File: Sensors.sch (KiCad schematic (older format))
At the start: 11 parts, among them Q20 2N7002K, Q21 2N7002K, U12 SHTC3

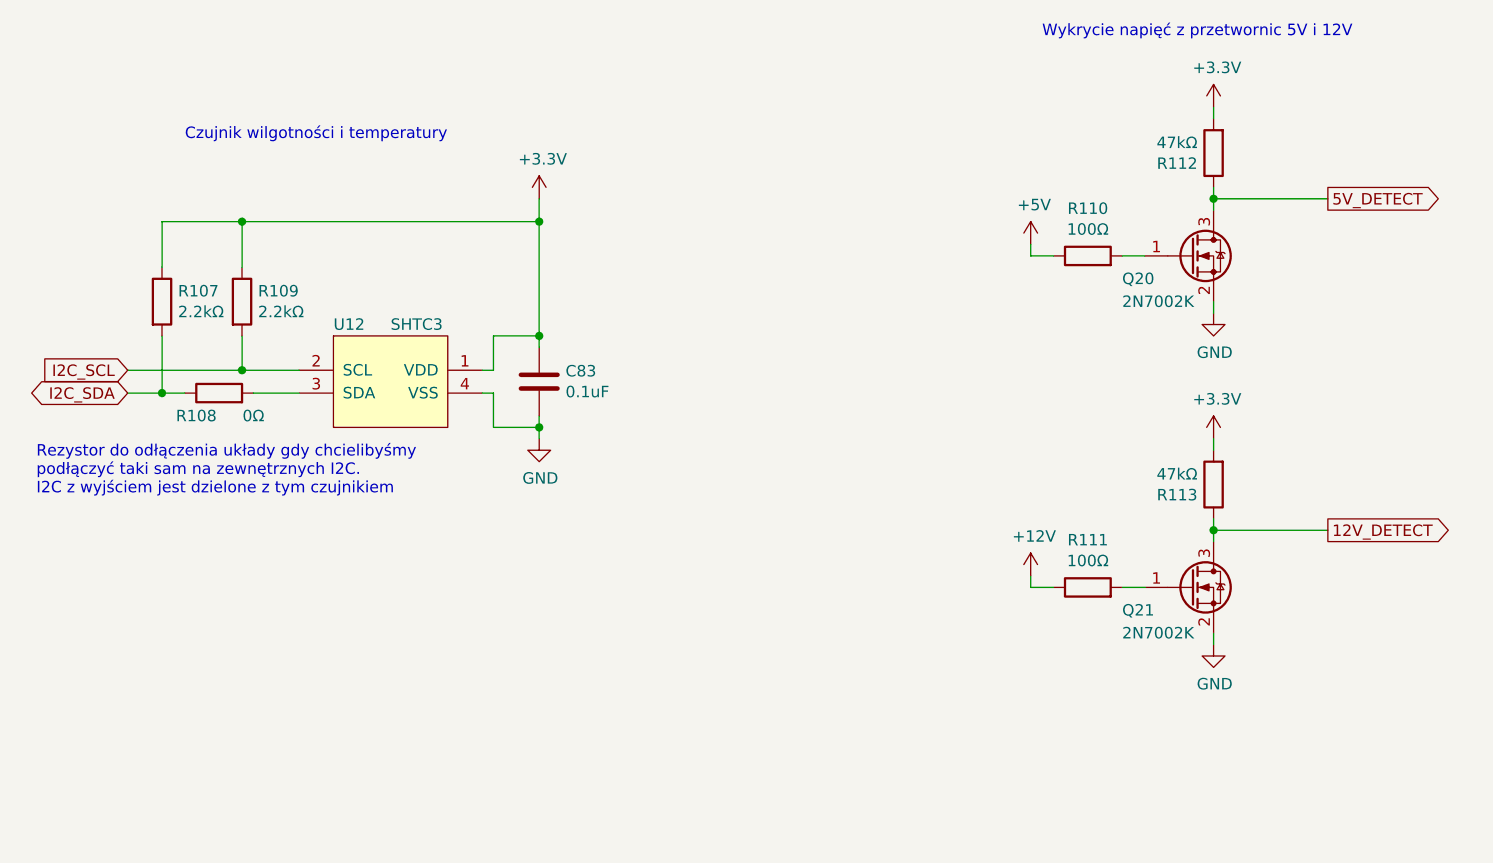
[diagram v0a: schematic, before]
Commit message: Improve ESD Protection for TMC2209, Fuses. Schematic ready v1
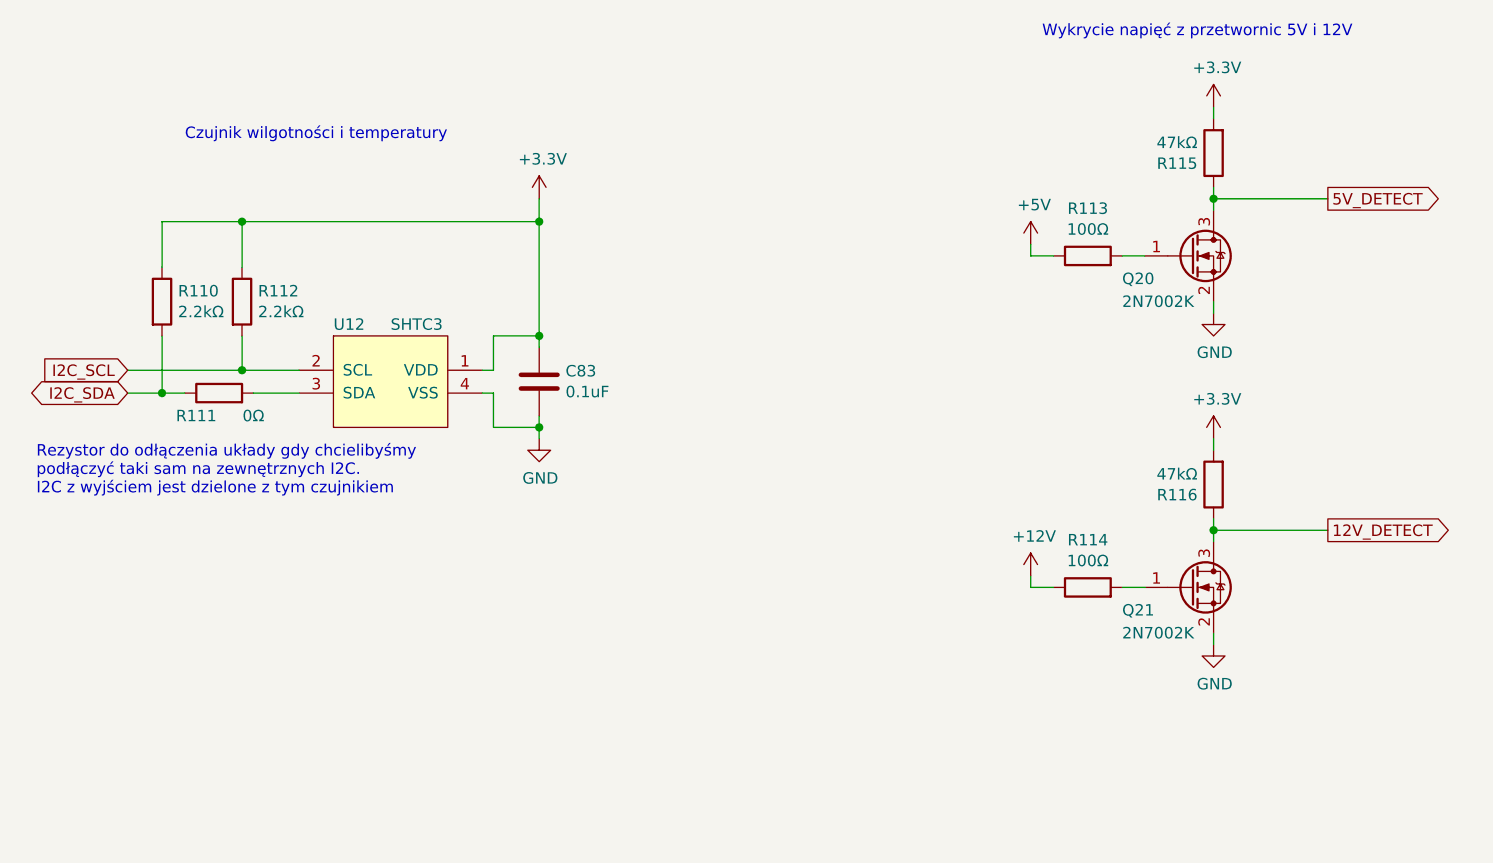
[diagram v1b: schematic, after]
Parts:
- renumbered R107 to R110, R108 to R111, R109 to R112, R110 to R113, R111 to R114, R112 to R115, R113 to R116
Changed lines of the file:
@@
 $EndComp
 $Comp
-L power:GND #PWR0217
+L power:GND #PWR0208
 U 1 1 5E15EB06
 P 3900 2700
-F 0 "#PWR0217" H 3900 2450 50  0001 C CNN
+F 0 "#PWR0208" H 3900 2450 50  0001 C CNN
 F 1 "GND" H 3905 2527 50  0000 C CNN
 F 2 "" H 3900 2700 50  0001 C CNN
@@
 $EndComp
 $Comp
-L power:+3.3V #PWR0216
+L power:+3.3V #PWR0207
 U 1 1 5E15FDB5
 P 3900 1650
-F 0 "#PWR0216" H 3900 1500 50  0001 C CNN
+F 0 "#PWR0207" H 3900 1500 50  0001 C CNN
 F 1 "+3.3V" H 3915 1823 50  0000 C CNN
 F 2 "" H 3900 1650 50  0001 C CNN
@@
 AR Path="/5E91D7CC/5E1C6F9E" Ref="R?"  Part="1"
 AR Path="/5E91D96F/5E1C6F9E" Ref="R?"  Part="1"
-AR Path="/5E1B3A8F/5E1C6F9E" Ref="R109"  Part="1"
-F 0 "R109" H 2670 2146 50  0000 L CNN
+AR Path="/5E1B3A8F/5E1C6F9E" Ref="R112"  Part="1"
+F 0 "R112" H 2670 2146 50  0000 L CNN
 F 1 "2.2kΩ" H 2670 2055 50  0000 L CNN
 F 2 "Resistor_SMD:R_0603_1608Metric" V 2530 2100 50  0001 C CNN
@@
 AR Path="/5E91D7CC/5E1C6FA4" Ref="R?"  Part="1"
 AR Path="/5E91D96F/5E1C6FA4" Ref="R?"  Part="1"
-AR Path="/5E1B3A8F/5E1C6FA4" Ref="R107"  Part="1"
-F 0 "R107" H 2320 2146 50  0000 L CNN
+AR Path="/5E1B3A8F/5E1C6FA4" Ref="R110"  Part="1"
+F 0 "R110" H 2320 2146 50  0000 L CNN
 F 1 "2.2kΩ" H 2320 2055 50  0000 L CNN
 F 2 "Resistor_SMD:R_0603_1608Metric" V 2180 2100 50  0001 C CNN
@@
 P 6850 1250
 AR Path="/5DFB2EC0/5E1CAE31" Ref="#PWR?"  Part="1"
-AR Path="/5E1B3A8F/5E1CAE31" Ref="#PWR0220"  Part="1"
-F 0 "#PWR0220" H 6850 1100 50  0001 C CNN
+AR Path="/5E1B3A8F/5E1CAE31" Ref="#PWR0211"  Part="1"
+F 0 "#PWR0211" H 6850 1100 50  0001 C CNN
 F 1 "+3.3V" H 6865 1423 50  0000 C CNN
 F 2 "" H 6850 1250 50  0001 C CNN
@@
 P 6850 2150
 AR Path="/5DFB2EC0/5E1CAE3F" Ref="#PWR?"  Part="1"
-AR Path="/5E1B3A8F/5E1CAE3F" Ref="#PWR0221"  Part="1"
-F 0 "#PWR0221" H 6850 1900 50  0001 C CNN
+AR Path="/5E1B3A8F/5E1CAE3F" Ref="#PWR0212"  Part="1"
+F 0 "#PWR0212" H 6850 1900 50  0001 C CNN
 F 1 "GND" H 6855 1977 50  0000 C CNN
 F 2 "" H 6850 2150 50  0001 C CNN
@@
 AR Path="/5E1018C2/5E1CAE4C" Ref="R?"  Part="1"
 AR Path="/5DFB2EC0/5E1CAE4C" Ref="R?"  Part="1"
-AR Path="/5E1B3A8F/5E1CAE4C" Ref="R112"  Part="1"
-F 0 "R112" H 6920 1496 50  0000 L CNN
+AR Path="/5E1B3A8F/5E1CAE4C" Ref="R115"  Part="1"
+F 0 "R115" H 6920 1496 50  0000 L CNN
 F 1 "47kΩ" H 6920 1405 50  0000 L CNN
 F 2 "Resistor_SMD:R_0603_1608Metric" V 6780 1450 50  0001 C CNN
@@
 AR Path="/5E07245F/5E1DC744" Ref="R?"  Part="1"
 AR Path="/5E858220/5E1DC744" Ref="R?"  Part="1"
-AR Path="/5E1B3A8F/5E1DC744" Ref="R110"  Part="1"
-F 0 "R110" V 6507 1900 50  0000 C CNN
+AR Path="/5E1B3A8F/5E1DC744" Ref="R113"  Part="1"
+F 0 "R113" V 6507 1900 50  0000 C CNN
 F 1 "100Ω" V 6416 1900 50  0000 C CNN
 F 2 "Resistor_SMD:R_0603_1608Metric" V 6230 1900 50  0001 C CNN
@@
 P 6850 2700
 AR Path="/5DFB2EC0/5E1DEF2F" Ref="#PWR?"  Part="1"
-AR Path="/5E1B3A8F/5E1DEF2F" Ref="#PWR0222"  Part="1"
-F 0 "#PWR0222" H 6850 2550 50  0001 C CNN
+AR Path="/5E1B3A8F/5E1DEF2F" Ref="#PWR0213"  Part="1"
+F 0 "#PWR0213" H 6850 2550 50  0001 C CNN
 F 1 "+3.3V" H 6865 2873 50  0000 C CNN
 F 2 "" H 6850 2700 50  0001 C CNN
@@
 P 6850 3600
 AR Path="/5DFB2EC0/5E1DEF45" Ref="#PWR?"  Part="1"
-AR Path="/5E1B3A8F/5E1DEF45" Ref="#PWR0223"  Part="1"
-F 0 "#PWR0223" H 6850 3350 50  0001 C CNN
+AR Path="/5E1B3A8F/5E1DEF45" Ref="#PWR0214"  Part="1"
+F 0 "#PWR0214" H 6850 3350 50  0001 C CNN
 F 1 "GND" H 6855 3427 50  0000 C CNN
 F 2 "" H 6850 3600 50  0001 C CNN
@@
 AR Path="/5E1018C2/5E1DEF56" Ref="R?"  Part="1"
 AR Path="/5DFB2EC0/5E1DEF56" Ref="R?"  Part="1"
-AR Path="/5E1B3A8F/5E1DEF56" Ref="R113"  Part="1"
-F 0 "R113" H 6920 2946 50  0000 L CNN
+AR Path="/5E1B3A8F/5E1DEF56" Ref="R116"  Part="1"
+F 0 "R116" H 6920 2946 50  0000 L CNN
 F 1 "47kΩ" H 6920 2855 50  0000 L CNN
 F 2 "Resistor_SMD:R_0603_1608Metric" V 6780 2900 50  0001 C CNN
@@
 AR Path="/5E07245F/5E1DEF71" Ref="R?"  Part="1"
 AR Path="/5E858220/5E1DEF71" Ref="R?"  Part="1"
-AR Path="/5E1B3A8F/5E1DEF71" Ref="R111"  Part="1"
-F 0 "R111" V 6507 3350 50  0000 C CNN
+AR Path="/5E1B3A8F/5E1DEF71" Ref="R114"  Part="1"
+F 0 "R114" V 6507 3350 50  0000 C CNN
 F 1 "100Ω" V 6416 3350 50  0000 C CNN
 F 2 "Resistor_SMD:R_0603_1608Metric" V 6230 3350 50  0001 C CNN
@@
 AR Path="/5E07245F/5E48B894" Ref="R?"  Part="1"
 AR Path="/5E858220/5E48B894" Ref="R?"  Part="1"
-AR Path="/5E1B3A8F/5E48B894" Ref="R108"  Part="1"
-F 0 "R108" V 2400 2600 50  0000 C CNN
+AR Path="/5E1B3A8F/5E48B894" Ref="R111"  Part="1"
+F 0 "R111" V 2400 2600 50  0000 C CNN
 F 1 "0Ω" V 2400 2350 50  0000 C CNN
 F 2 "Resistor_SMD:R_0603_1608Metric" V 2430 2500 50  0001 C CNN
@@
 Connection ~ 2250 2500
 $Comp
-L power:+5V #PWR0218
+L power:+5V #PWR0209
 U 1 1 5E509315
 P 6050 1850
-F 0 "#PWR0218" H 6050 1700 50  0001 C CNN
+F 0 "#PWR0209" H 6050 1700 50  0001 C CNN
 F 1 "+5V" H 6065 2023 50  0000 C CNN
 F 2 "" H 6050 1850 50  0001 C CNN
@@
 $EndComp
 $Comp
-L power:+12V #PWR0219
+L power:+12V #PWR0210
 U 1 1 5E509AAF
 P 6050 3300
-F 0 "#PWR0219" H 6050 3150 50  0001 C CNN
+F 0 "#PWR0210" H 6050 3150 50  0001 C CNN
 F 1 "+12V" H 6065 3473 50  0000 C CNN
 F 2 "" H 6050 3300 50  0001 C CNN

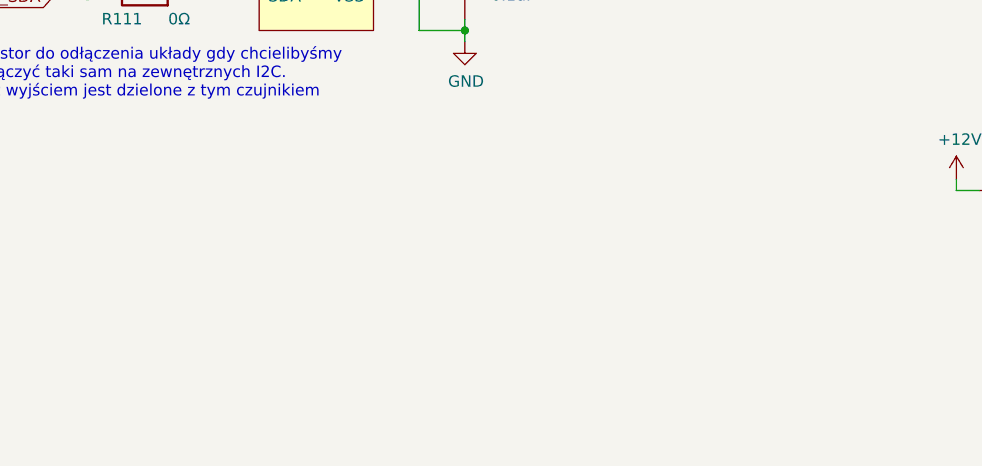
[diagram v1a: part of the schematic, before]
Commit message: Added EEPROM on schematic
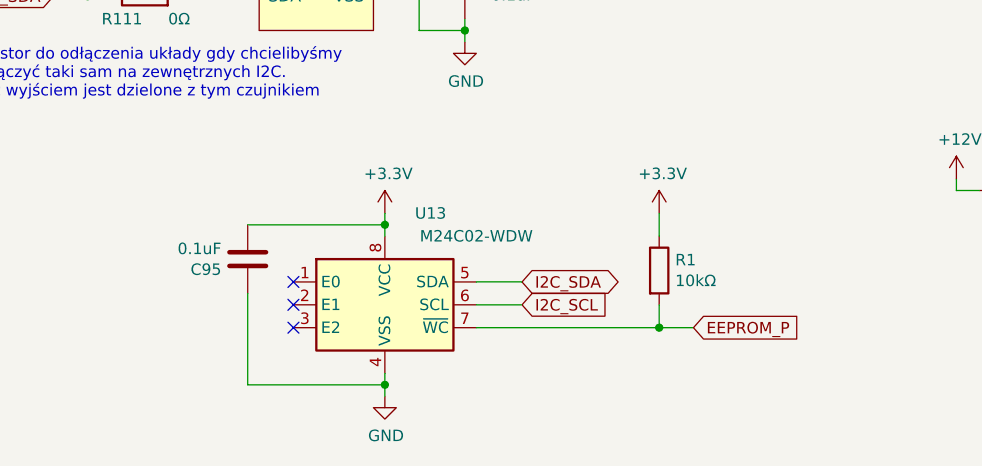
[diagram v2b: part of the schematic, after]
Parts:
- added C95: 0.1uF, Capacitor_SMD:C_0603_1608Metric, symbol Device:C
- added R1: 10kΩ, Resistor_SMD:R_0603_1608Metric, symbol Device:R
- added U13: M24C02-WDW, Package_SO:TSSOP-8_4.4x3mm_P0.65mm, symbol Memory_EEPROM:M24C02-WDW
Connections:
- net +3V3: now also C95.2, R1.1, U13.8 (VCC)
- net GND: now also C95.1, U13.4 (VSS)
- net I2C_SCL: now also U13.6 (SCL)
- net I2C_SDA: now also U13.5 (SDA)
- new net EEPROM_P: R1.2, U13.7 (~WC)
- no-connect marks 0 -> 3
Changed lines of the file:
@@
 Text Notes 1700 2950 0    50   ~ 0
 Rezystor do odłączenia układy gdy chcielibyśmy\npodłączyć taki sam na zewnętrznych I2C.\nI2C z wyjściem jest dzielone z tym czujnikiem
+$Comp
+L Memory_EEPROM:M24C02-WDW U13
+U 1 1 5E2A2C9E
+P 3550 3850
+F 0 "U13" H 3750 4250 50  0000 C CNN
+F 1 "M24C02-WDW" H 3950 4150 50  0000 C CNN
+F 2 "Package_SO:TSSOP-8_4.4x3mm_P0.65mm" H 3550 4200 50  0001 C CNN
+F 3 "http://www.st.com/content/ccc/resource/technical/document/datasheet/b0/d8/50/40/5a/85/49/6f/DM00071904.pdf/files/DM00071904.pdf/jcr:content/translations/en.DM00071904.pdf" H 3600 3350 50  0001 C CNN
+	1    3550 3850
+	1    0    0    -1
+$EndComp
+NoConn ~ 3150 3750
+NoConn ~ 3150 3850
+NoConn ~ 3150 3950
+$Comp
+L Device:R R?
+U 1 1 5E2A6608
+P 4750 3700
+AR Path="/5E91D7CC/5E2A6608" Ref="R?"  Part="1"
+AR Path="/5E91D96F/5E2A6608" Ref="R?"  Part="1"
+AR Path="/5E1B3A8F/5E2A6608" Ref="R1"  Part="1"
+F 0 "R1" H 4820 3746 50  0000 L CNN
+F 1 "10kΩ" H 4820 3655 50  0000 L CNN
+F 2 "Resistor_SMD:R_0603_1608Metric" V 4680 3700 50  0001 C CNN
+F 3 "~" H 4750 3700 50  0001 C CNN
+F 4 "0.04651" H 4750 3700 50  0001 C CNN "Cena"
+F 5 "SMD" H 4750 3700 50  0001 C CNN "Typ"
+	1    4750 3700
+	1    0    0    -1
+$EndComp
+Text GLabel 4150 3850 2    50   Input ~ 0
+I2C_SCL
+Text GLabel 4150 3750 2    50   BiDi ~ 0
+I2C_SDA
+Wire Wire Line
+	3950 3750 4150 3750
+Wire Wire Line
+	3950 3850 4150 3850
+$Comp
+L power:GND #PWR0221
+U 1 1 5E2A9FA2
+P 3550 4250
+F 0 "#PWR0221" H 3550 4000 50  0001 C CNN
+F 1 "GND" H 3555 4077 50  0000 C CNN
+F 2 "" H 3550 4250 50  0001 C CNN
+F 3 "" H 3550 4250 50  0001 C CNN
+	1    3550 4250
+	1    0    0    -1
+$EndComp
+$Comp
+L power:+3.3V #PWR0222
+U 1 1 5E2AA2F7
+P 3550 3450
+F 0 "#PWR0222" H 3550 3300 50  0001 C CNN
+F 1 "+3.3V" H 3565 3623 50  0000 C CNN
+F 2 "" H 3550 3450 50  0001 C CNN
+F 3 "" H 3550 3450 50  0001 C CNN
+	1    3550 3450
+	1    0    0    -1
+$EndComp
+Wire Wire Line
+	3550 3450 3550 3500
+Wire Wire Line
+	3550 3500 2950 3500
+Connection ~ 3550 3500
+Wire Wire Line
+	3550 3500 3550 3550
+Wire Wire Line
+	2950 3800 2950 4200
+Wire Wire Line
+	2950 4200 3550 4200
+Wire Wire Line
+	3550 4200 3550 4150
+Wire Wire Line
+	3550 4200 3550 4250
+Connection ~ 3550 4200
+$Comp
+L power:+3.3V #PWR0223
+U 1 1 5E2AF48A
+P 4750 3450
+F 0 "#PWR0223" H 4750 3300 50  0001 C CNN
+F 1 "+3.3V" H 4765 3623 50  0000 C CNN
+F 2 "" H 4750 3450 50  0001 C CNN
+F 3 "" H 4750 3450 50  0001 C CNN
+	1    4750 3450
+	1    0    0    -1
+$EndComp
+Wire Wire Line
+	4750 3450 4750 3550
+Wire Wire Line
+	4750 3950 4750 3850
+Wire Wire Line
+	3950 3950 4750 3950
+Wire Wire Line
+	4750 3950 4900 3950
+Connection ~ 4750 3950
+$Comp
+L Device:C C95
+U 1 1 5E2B5185
+P 2950 3650
+F 0 "C95" H 3065 3696 50  0000 L CNN
+F 1 "0.1uF" H 3065 3605 50  0000 L CNN
+F 2 "Capacitor_SMD:C_0603_1608Metric" H 2988 3500 50  0001 C CNN
+F 3 "~" H 2950 3650 50  0001 C CNN
+F 4 "0.05982" H 2950 3650 50  0001 C CNN "Cena"
+F 5 "CL10B104KB8NNNC " H 2950 3650 50  0001 C CNN "Model"
+F 6 "50V" H 2950 3650 50  0001 C CNN "Napięcie"
+F 7 "SAMSUNG" H 2950 3650 50  0001 C CNN "Producent"
+F 8 "10%" H 2950 3650 50  0001 C CNN "Tolerancja"
+F 9 "SMD" H 2950 3650 50  0001 C CNN "Typ"
+	1    2950 3650
+	-1   0    0    1
+$EndComp
+Text GLabel 4900 3950 2    50   Input ~ 0
+EEPROM_P
 $EndSCHEMATC
